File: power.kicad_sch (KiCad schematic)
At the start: 28 parts, among them U21 TPS62A06DRLR, U23 INA187A2IDBVR, U24 INA228AQDGSRQ1

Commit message: [#98577] Unify LEDs
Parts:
- D17: value LED_G_0603_LTST-C190GKT -> LED_G_0603_LG_L29K-G2J1-24-Z; symbol antmicroLEDIndicationDiscrete:LED_G_0603_LTST-C190GKT -> antmicroLEDIndicationDiscrete:LED_G_0603_LG_L29K-G2J1-24-Z; MPN LTST-C190GKT -> LG L29K-G2J1-24-Z; Manufacturer Lite-On -> OSRAM
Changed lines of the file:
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@@
 	)
 	(symbol
-		(lib_id "antmicroLEDIndicationDiscrete:LED_G_0603_LTST-C190GKT")
+		(lib_id "antmicroLEDIndicationDiscrete:LED_G_0603_LG_L29K-G2J1-24-Z")
 		(at 154.94 234.95 180)
 		(unit 1)
@@
 			)
 		)
-		(property "Value" "LED_G_0603_LTST-C190GKT"
-			(at 132.08 227.33 0)
+		(property "Value" "LED_G_0603_LG_L29K-G2J1-24-Z"
+			(at 134.62 227.33 0)
 			(effects
 				(font
@@
 		)
 		(property "Footprint" "antmicro-footprints:LED_0603_1608Metric_G"
-			(at 132.08 224.79 0)
+			(at 134.62 224.79 0)
 			(effects
 				(font
@@
 			)
 		)
-		(property "Datasheet" "https://media.digikey.com/pdf/Data%20Sheets/Lite-On%20PDFs/LTST-C190GKT.pdf"
-			(at 132.08 222.25 0)
+		(property "Datasheet" "https://look.ams-osram.com/m/19ee86b3ae0ee95b/original/LG-L29K.pdf"
+			(at 134.62 222.25 0)
 			(effects
 				(font
@@
 			)
 		)
-		(property "Description" "LED, Green, SMD, 0603, 20 mA, 2.1 V, 569 nm"
-			(at 132.08 209.55 0)
+		(property "Description" "LED, Green, SMD, 0603, 20 mA, 1.7 V, 570 nm"
+			(at 134.62 209.55 0)
 			(effects
 				(font
@@
 			)
 		)
-		(property "MPN" "LTST-C190GKT"
-			(at 132.08 219.71 0)
+		(property "MPN" "LG L29K-G2J1-24-Z"
+			(at 134.62 219.71 0)
 			(effects
 				(font
@@
 			)
 		)
-		(property "Manufacturer" "Lite-On"
-			(at 132.08 217.17 0)
+		(property "Manufacturer" "OSRAM"
+			(at 134.62 217.17 0)
 			(effects
 				(font
@@
 		)
 		(property "Author" "Antmicro"
-			(at 132.08 214.63 0)
+			(at 134.62 214.63 0)
 			(effects
 				(font
@@
 		)
 		(property "License" "Apache-2.0"
-			(at 132.08 212.09 0)
+			(at 134.62 212.09 0)
 			(effects
 				(font

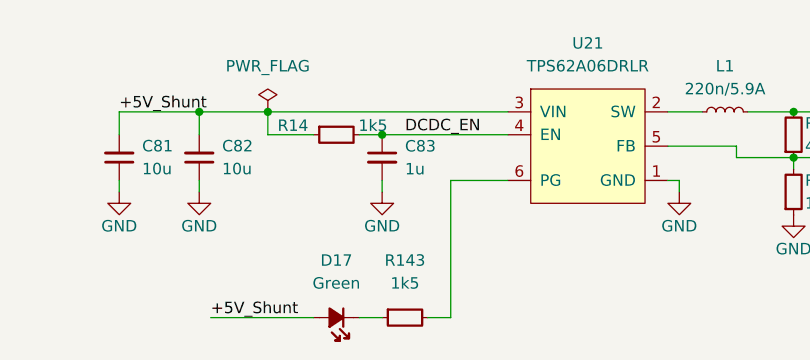
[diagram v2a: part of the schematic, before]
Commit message: [#98577] Unify LED Resistor values
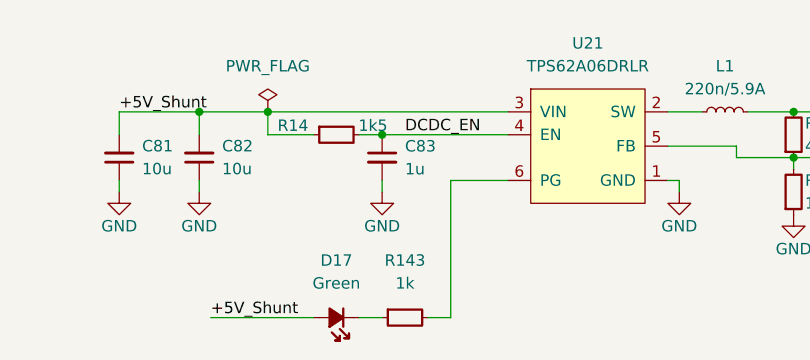
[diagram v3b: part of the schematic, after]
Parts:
- R143: value R_1k5_0402 -> R_1k_0402; symbol antmicroResistors0402:R_1k5_0402 -> antmicroResistors0402:R_1k_0402; MPN CR0402-FX-1501GLF -> CR0402-FX-1001GLF; Val 1k5 -> 1k
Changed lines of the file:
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@@
 	)
 	(symbol
-		(lib_id "antmicroResistors0402:R_1k5_0402")
+		(lib_id "antmicroResistors0402:R_1k_0402")
 		(at 157.48 234.95 0)
 		(unit 1)
@@
 			)
 		)
-		(property "Value" "R_1k5_0402"
+		(property "Value" "R_1k_0402"
 			(at 177.8 247.65 0)
 			(effects
@@
 			)
 		)
-		(property "Description" "SMD Chip Resistor, 1.5 kohm, ± 1%, 62.5 mW, 0402 [1005 Metric], Thick Film, General Purpose"
+		(property "Description" "SMD Chip Resistor, 1 kohm, ± 1%, 63 mW, 0402 [1005 Metric], Thick Film, General Purpose"
 			(at 177.8 265.43 0)
 			(effects
@@
 			)
 		)
-		(property "MPN" "CR0402-FX-1501GLF"
+		(property "MPN" "CR0402-FX-1001GLF"
 			(at 177.8 255.27 0)
 			(effects
@@
 			)
 		)
-		(property "Val" "1k5"
+		(property "Val" "1k"
 			(at 160.02 231.14 0)
 			(effects

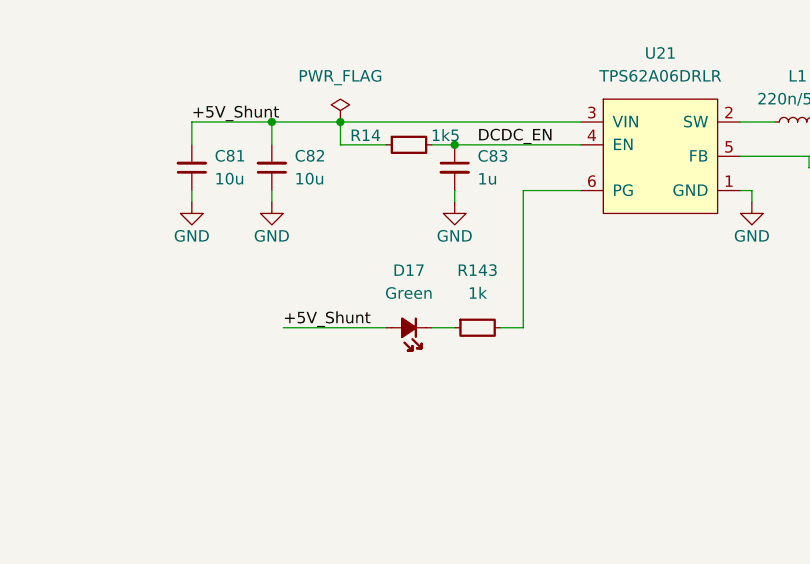
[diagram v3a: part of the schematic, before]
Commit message: [#98579] Fix PG LED logic and add LED description
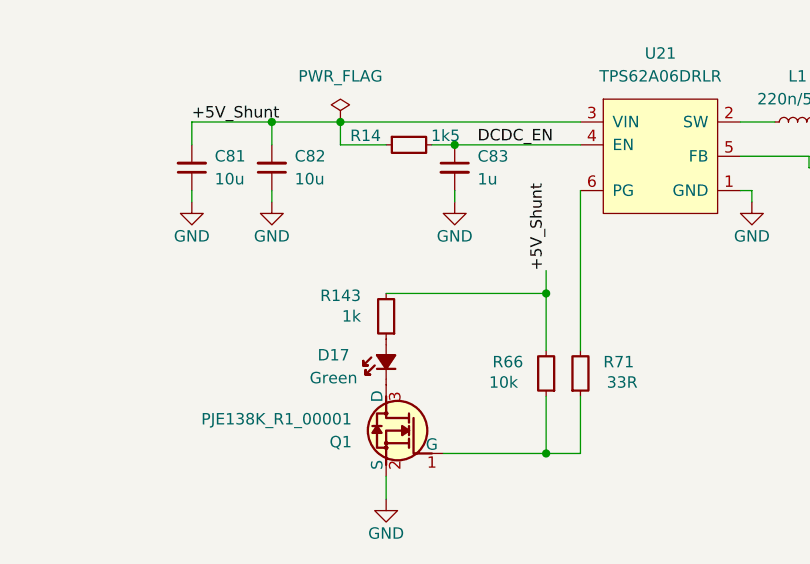
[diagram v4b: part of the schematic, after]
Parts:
- added Q1: PJE138K, antmicro-footprints:SOT-523, symbol antmicroTransistorsFETsMOSFETsSingle:PJE138K
- added R66: R_10k_0402, antmicro-footprints:R_0402_1005Metric, symbol antmicroResistors0402:R_10k_0402
- added R71: R_33R_0402, antmicro-footprints:R_0402_1005Metric, symbol antmicroResistors0402:R_33R_0402
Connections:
- net +5V_Shunt: now also R143.2, R66.2; no longer D17.2 (A)
- net GND: now also Q1.2 (S)
- net at D17.1 (C): now also Q1.3 (D); no longer R143.1
- net at U21.6 (PG): now also R71.2; no longer R143.2
- new net: Q1.1 (G), R66.1, R71.1
- new net: D17.2 (A), R143.1
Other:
- moved on the sheet: D17, R143
